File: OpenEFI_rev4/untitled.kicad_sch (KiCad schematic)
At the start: 32 parts, among them Q12 AO3400A, SW4 SW_DIP_x02, U36 MAX9926UAEE+

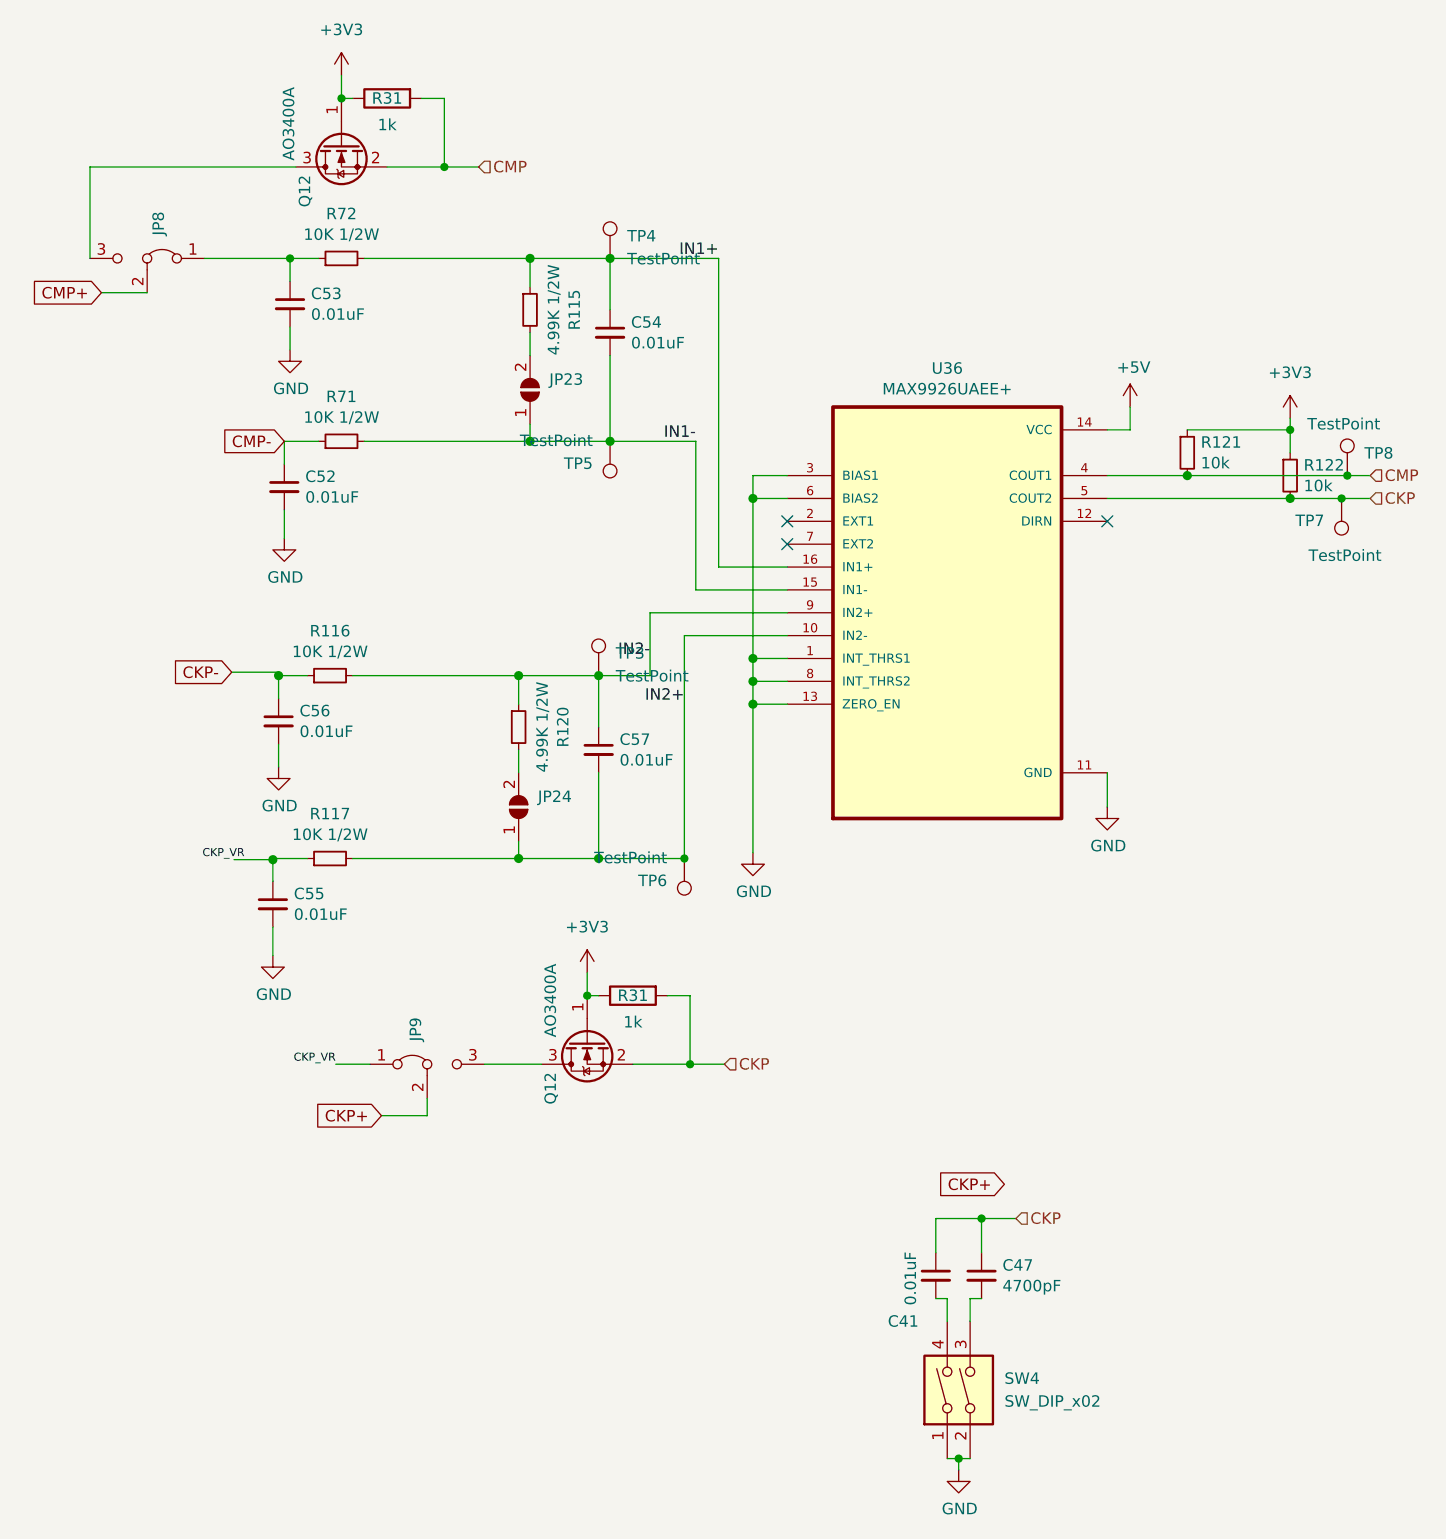
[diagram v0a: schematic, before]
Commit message: update 32khz crystal
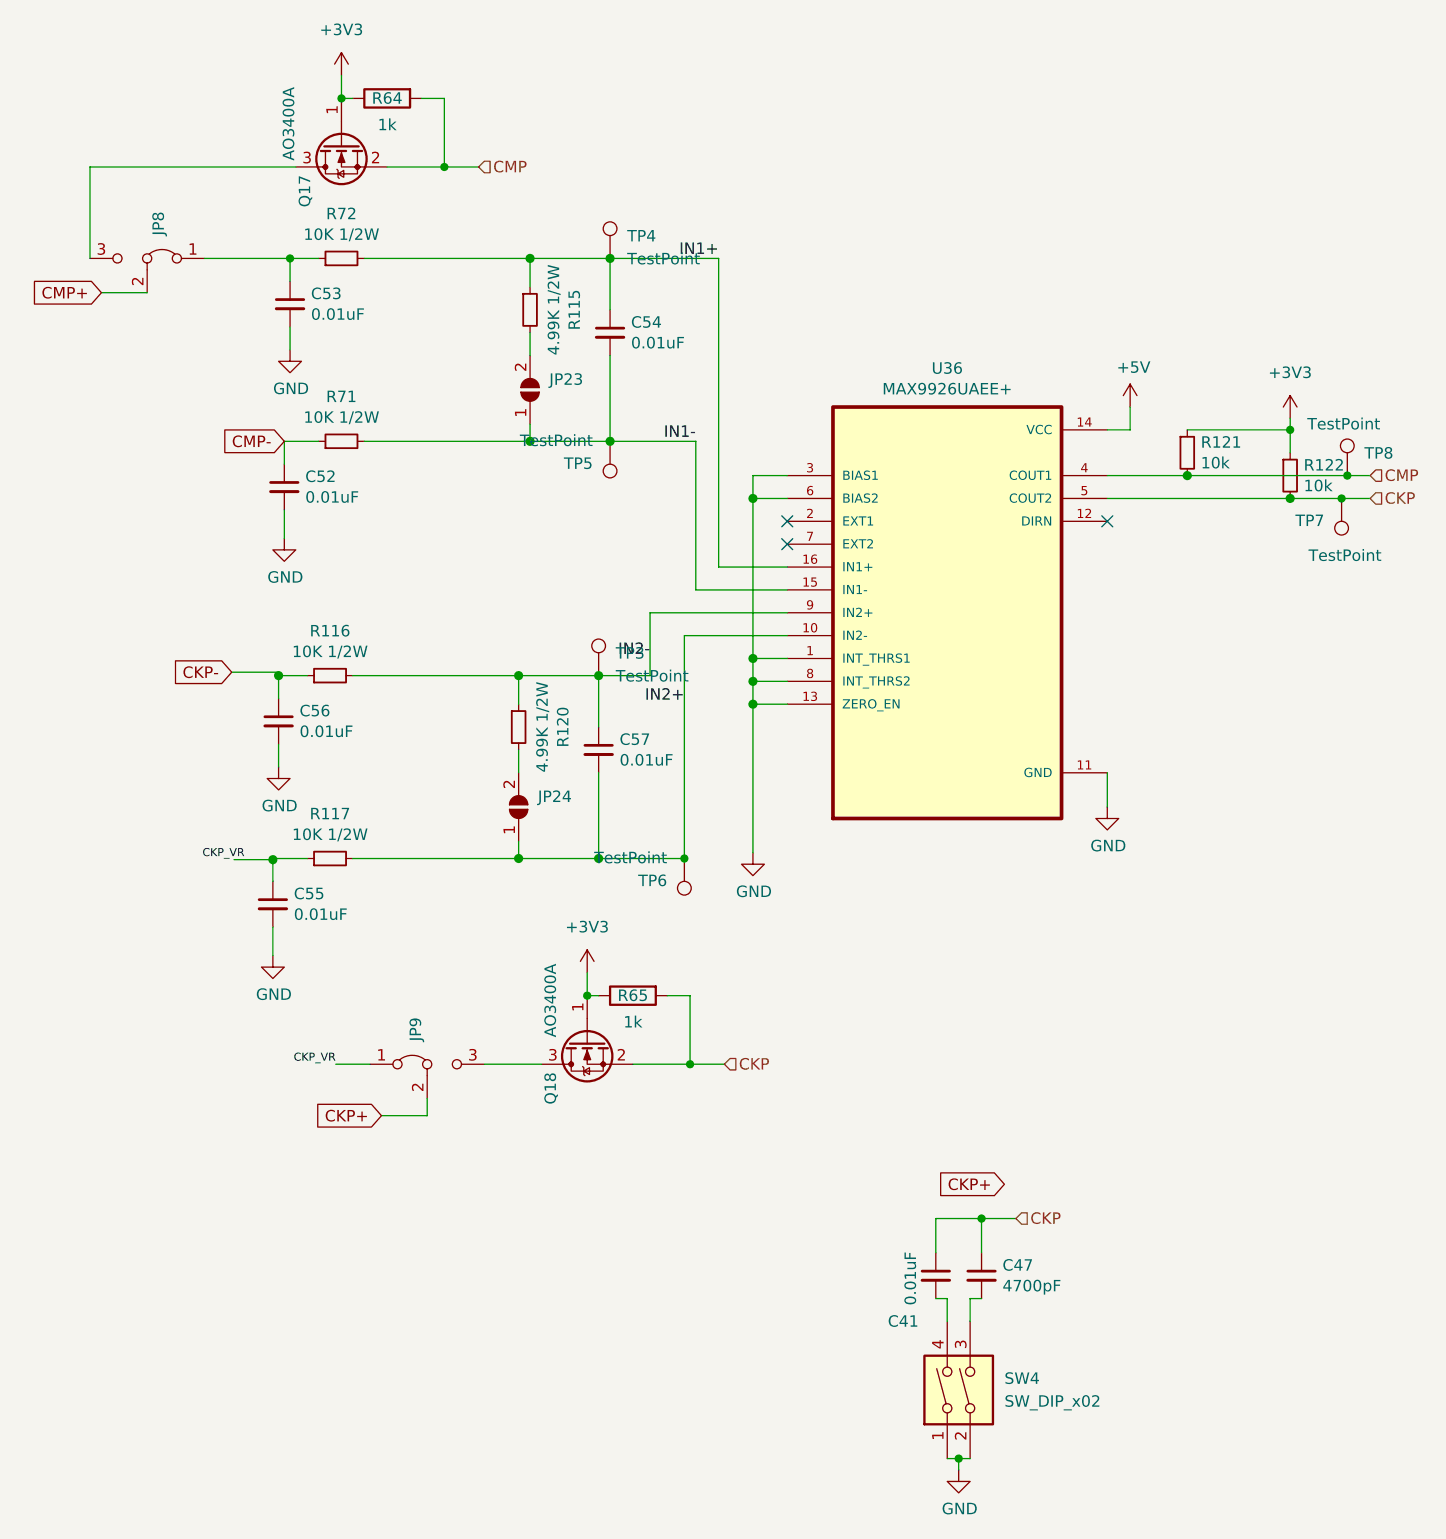
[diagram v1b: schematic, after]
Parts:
- renumbered Q12 to Q17, Q12 to Q18, R31 to R64, R31 to R65
